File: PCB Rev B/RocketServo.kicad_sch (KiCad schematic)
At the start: 30 parts, among them IC1 PIC12F1822-I/P, P1 Conn_01x02, P2 Conn_01x03, P3 Conn_01x02, SW1 Conn_01x02, SW2 Conn_01x02, U1 L7805, U2 TLP227GN

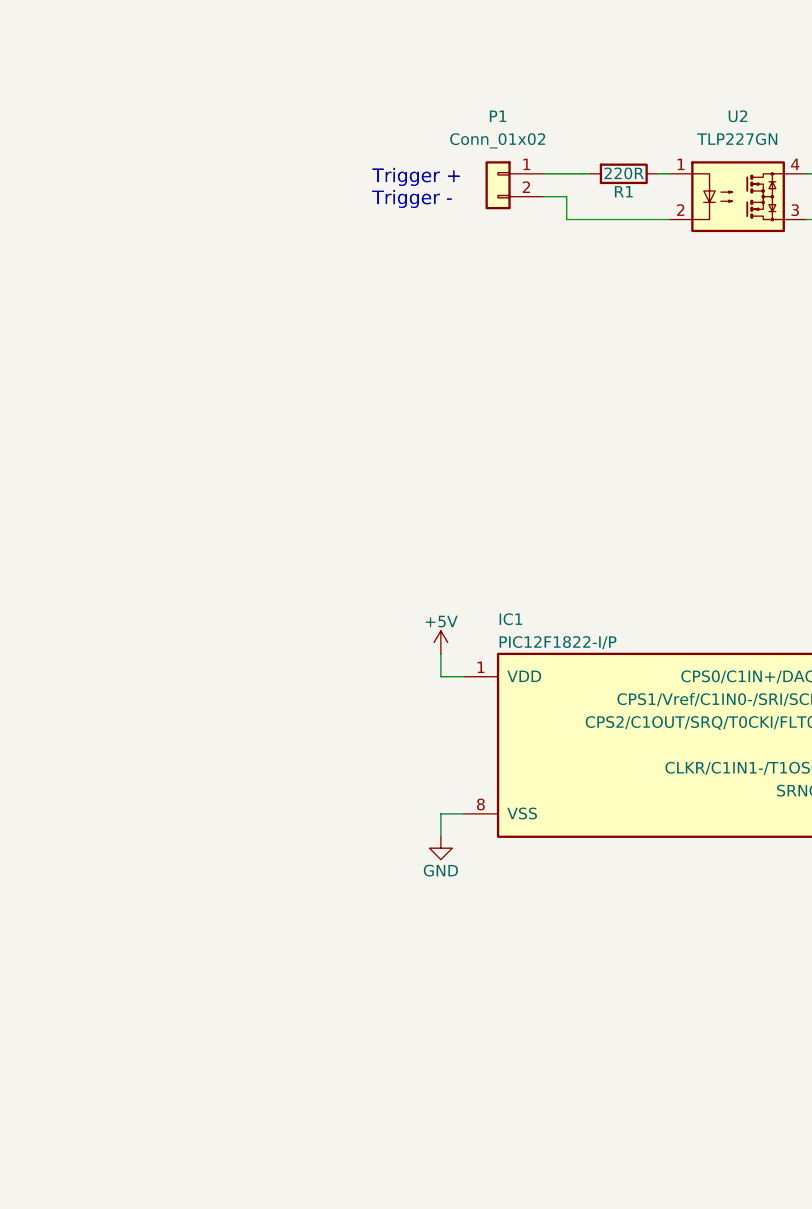
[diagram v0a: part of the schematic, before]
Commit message: Added parts list to sch
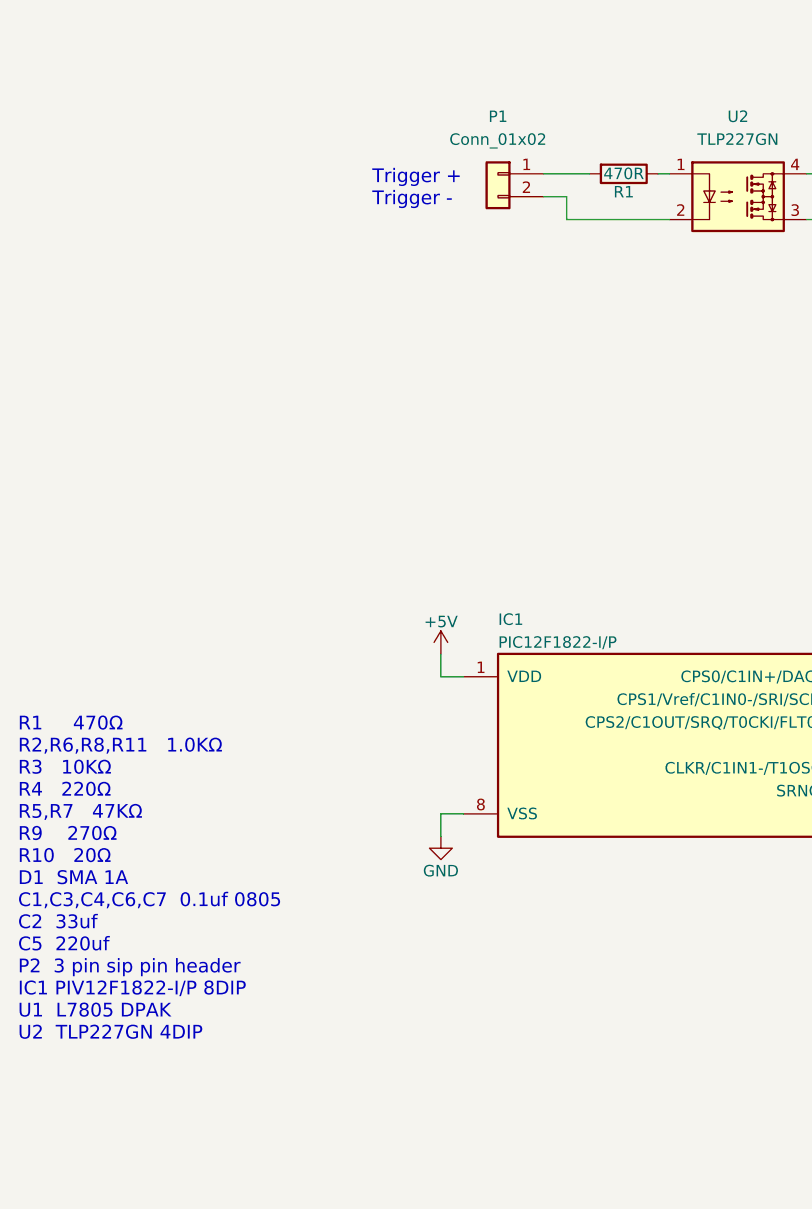
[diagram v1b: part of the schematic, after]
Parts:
- R1: value 220R -> 470R
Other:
- note added: "R1 470Ω R2,R6,R8,R11 1.0KΩ R3 10KΩ R4 220Ω R5,R7 47KΩ R9 270Ω R10 20Ω D1 SMA 1A C1,C3,C4,C6,C7 0.1uf 0805 C2 33uf C5 220uf P2 3 pin sip pin header IC1 PIV12F1822-I/P 8DIP U1 L7805 DPAK U2 TLP227GN 4DIP"
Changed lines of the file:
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@@
+    (effects (font (size 1.524 1.524)) (justify left bottom))
+  )
+  (text "R1     470Ω\nR2,R6,R8,R11   1.0KΩ\nR3   10KΩ\nR4   220Ω\nR5,R7   47KΩ\nR9    270Ω\nR10   20Ω\nD1  SMA 1A\nC1,C3,C4,C6,C7  0.1uf 0805\nC2  33uf\nC5  220uf\nP2  3 pin sip pin header\nIC1 PIV12F1822-I/P 8DIP\nU1  L7805 DPAK\nU2  TLP227GN 4DIP\n"
+    (at 25.4 157.48 0)
     (effects (font (size 1.524 1.524)) (justify left bottom))
   )
@@
     (in_bom yes) (on_board yes)
     (property "Reference" "R1" (id 0) (at 92.71 62.992 90))
-    (property "Value" "220R" (id 1) (at 92.71 60.96 90))
+    (property "Value" "470R" (id 1) (at 92.71 60.96 90))
     (property "Footprint" "Resistor_SMD:R_0805_2012Metric_Pad1.20x1.40mm_HandSolder" (id 2) (at 92.71 59.182 90)
       (effects (font (size 0.762 0.762)) hide)
@@
     )
     (path "/f42c9677-46fb-435d-8133-20b9ca51e3dc"
-      (reference "R1") (unit 1) (value "220R") (footprint "Resistor_SMD:R_0805_2012Metric_Pad1.20x1.40mm_HandSolder")
+      (reference "R1") (unit 1) (value "470R") (footprint "Resistor_SMD:R_0805_2012Metric_Pad1.20x1.40mm_HandSolder")
     )
     (path "/00000000-0000-0000-0000-00005615ef3d"

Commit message: notes
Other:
- note added: "R1 470Ω R2,R6,R8,R11 1.0KΩ R3 10KΩ R4 220Ω R5,R7 47KΩ R9 270Ω R10 20KΩ D1 SMA 1A C1,C3,C4,C6,C7 0.1uf 0805 C2 33uf C5 220uf P2 3 pin sip pin header IC1 PIV12F1822-I/P 8DIP U1 L7805 DPAK U2 TLP227GN 4DIP"
- note removed: "R1 470Ω R2,R6,R8,R11 1.0KΩ R3 10KΩ R4 220Ω R5,R7 47KΩ R9 270Ω R10 20Ω D1 SMA 1A C1,C3,C4,C6,C7 0.1uf 0805 C2 33uf C5 220uf P2 3 pin sip pin header IC1 PIV12F1822-I/P 8DIP U1 L7805 DPAK U2 TLP227GN 4DIP"

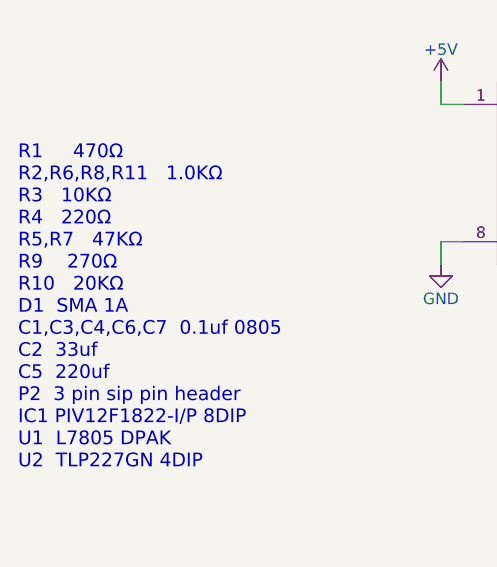
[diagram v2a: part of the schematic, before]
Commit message: R10 to 22K
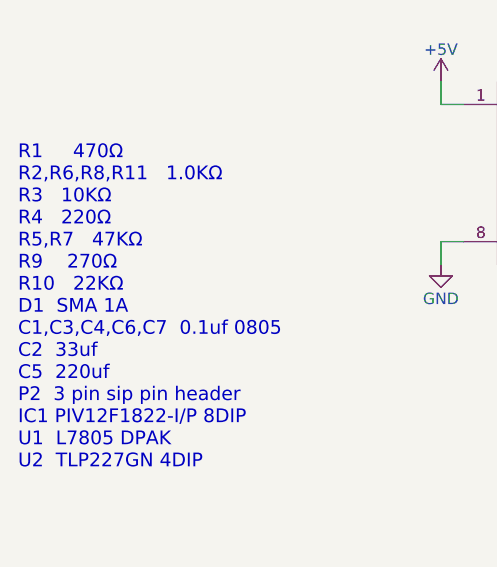
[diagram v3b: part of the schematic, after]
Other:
- note added: "R1 470Ω R2,R6,R8,R11 1.0KΩ R3 10KΩ R4 220Ω R5,R7 47KΩ R9 270Ω R10 22KΩ D1 SMA 1A C1,C3,C4,C6,C7 0.1uf 0805 C2 33uf C5 220uf P2 3 pin sip pin header IC1 PIV12F1822-I/P 8DIP U1 L7805 DPAK U2 TLP227GN 4DIP"
- note removed: "R1 470Ω R2,R6,R8,R11 1.0KΩ R3 10KΩ R4 220Ω R5,R7 47KΩ R9 270Ω R10 20KΩ D1 SMA 1A C1,C3,C4,C6,C7 0.1uf 0805 C2 33uf C5 220uf P2 3 pin sip pin header IC1 PIV12F1822-I/P 8DIP U1 L7805 DPAK U2 TLP227GN 4DIP"
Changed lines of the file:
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@@
     (effects (font (size 1.524 1.524)) (justify left bottom))
   )
-  (text "R1     470Ω\nR2,R6,R8,R11   1.0KΩ\nR3   10KΩ\nR4   220Ω\nR5,R7   47KΩ\nR9    270Ω\nR10   20KΩ\nD1  SMA 1A\nC1,C3,C4,C6,C7  0.1uf 0805\nC2  33uf\nC5  220uf\nP2  3 pin sip pin header\nIC1 PIV12F1822-I/P 8DIP\nU1  L7805 DPAK\nU2  TLP227GN 4DIP\n"
+  (text "R1     470Ω\nR2,R6,R8,R11   1.0KΩ\nR3   10KΩ\nR4   220Ω\nR5,R7   47KΩ\nR9    270Ω\nR10   22KΩ\nD1  SMA 1A\nC1,C3,C4,C6,C7  0.1uf 0805\nC2  33uf\nC5  220uf\nP2  3 pin sip pin header\nIC1 PIV12F1822-I/P 8DIP\nU1  L7805 DPAK\nU2  TLP227GN 4DIP\n"
     (at 25.4 157.48 0)
     (effects (font (size 1.524 1.524)) (justify left bottom))
